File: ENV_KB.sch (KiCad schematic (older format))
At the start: 224 parts, among them J1 TYPE-C-31-M-12, J2 Conn_01x03, U1 MCP23017_SP

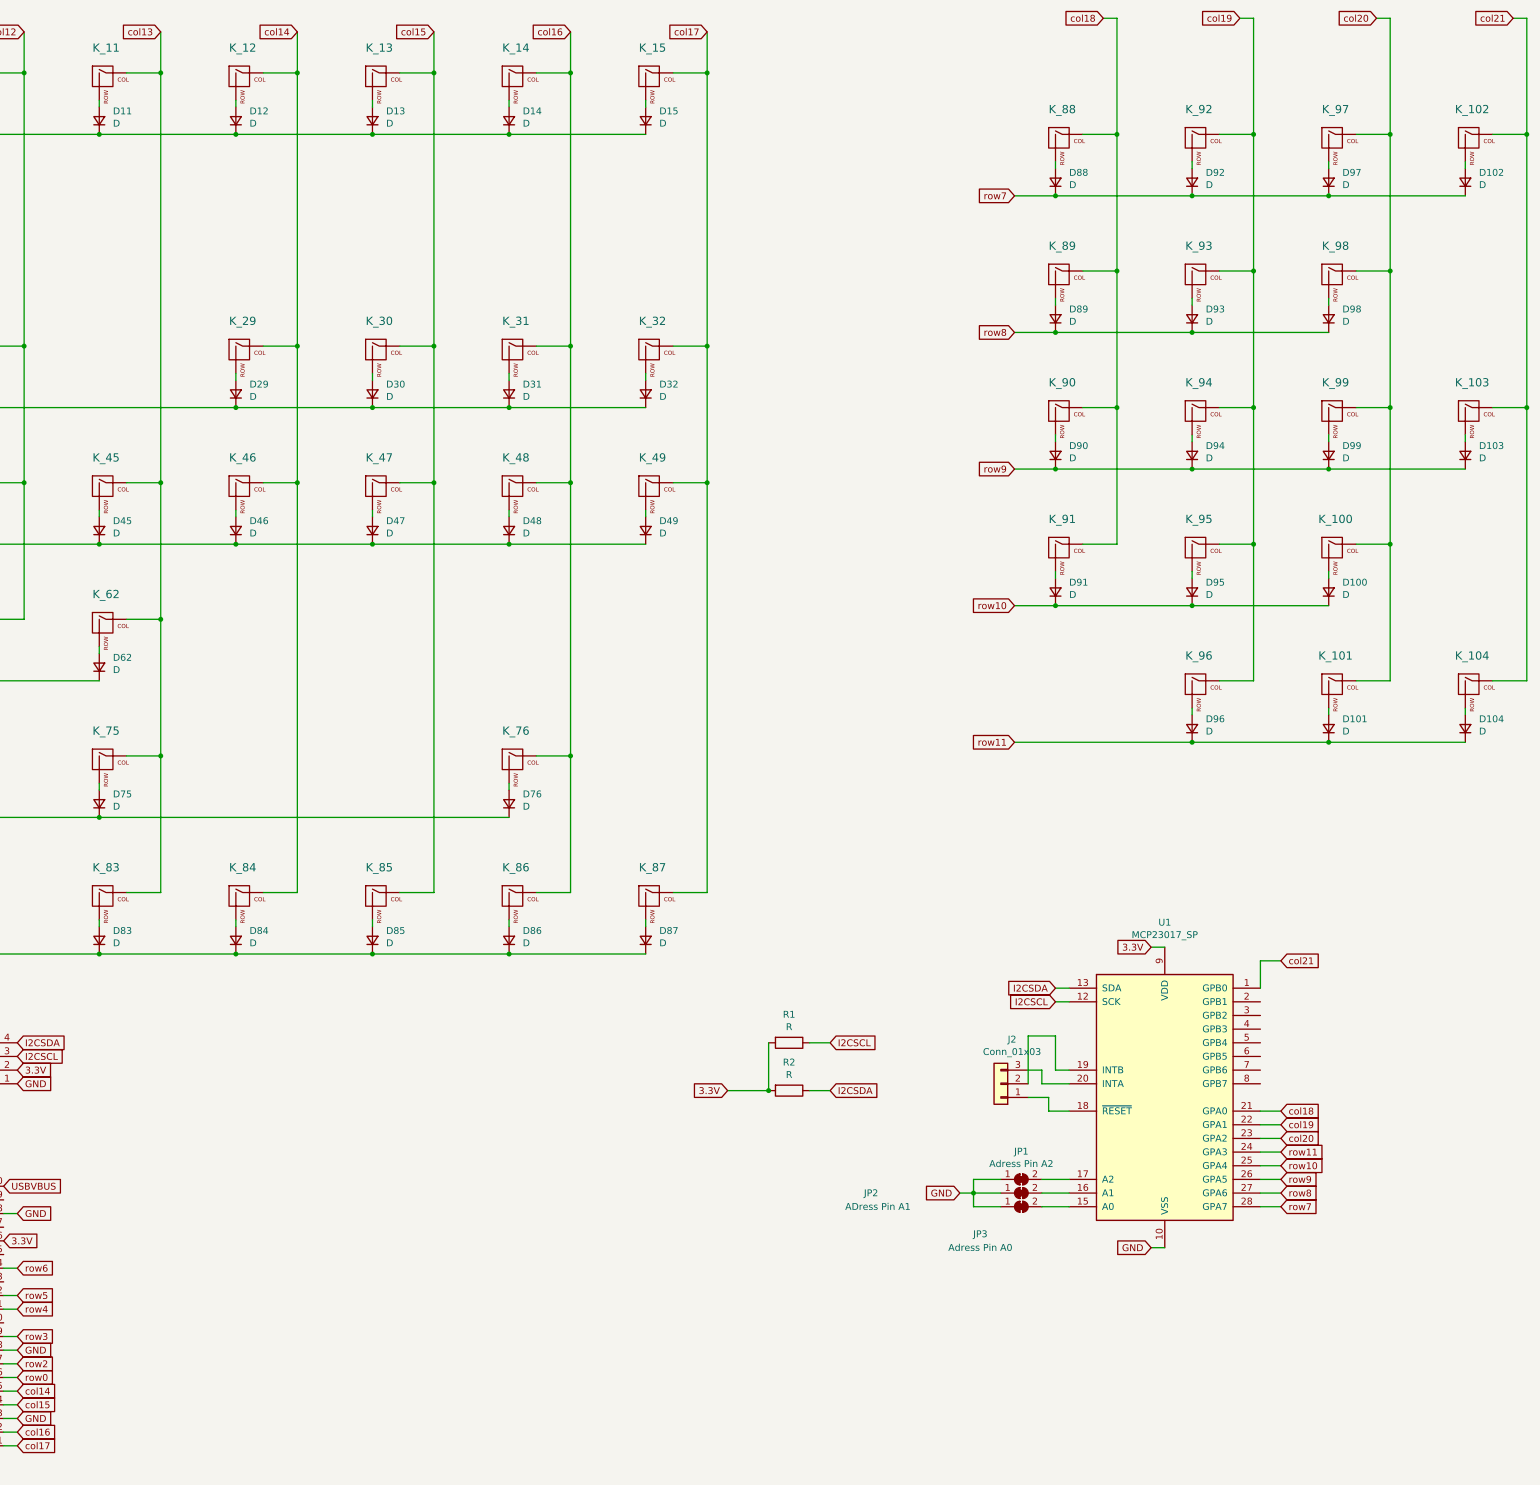
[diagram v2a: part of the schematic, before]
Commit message: Change: chaning schematic to use rows of main keyboard to save boot time TODO: Rerunning of the tracks to comply with schematic
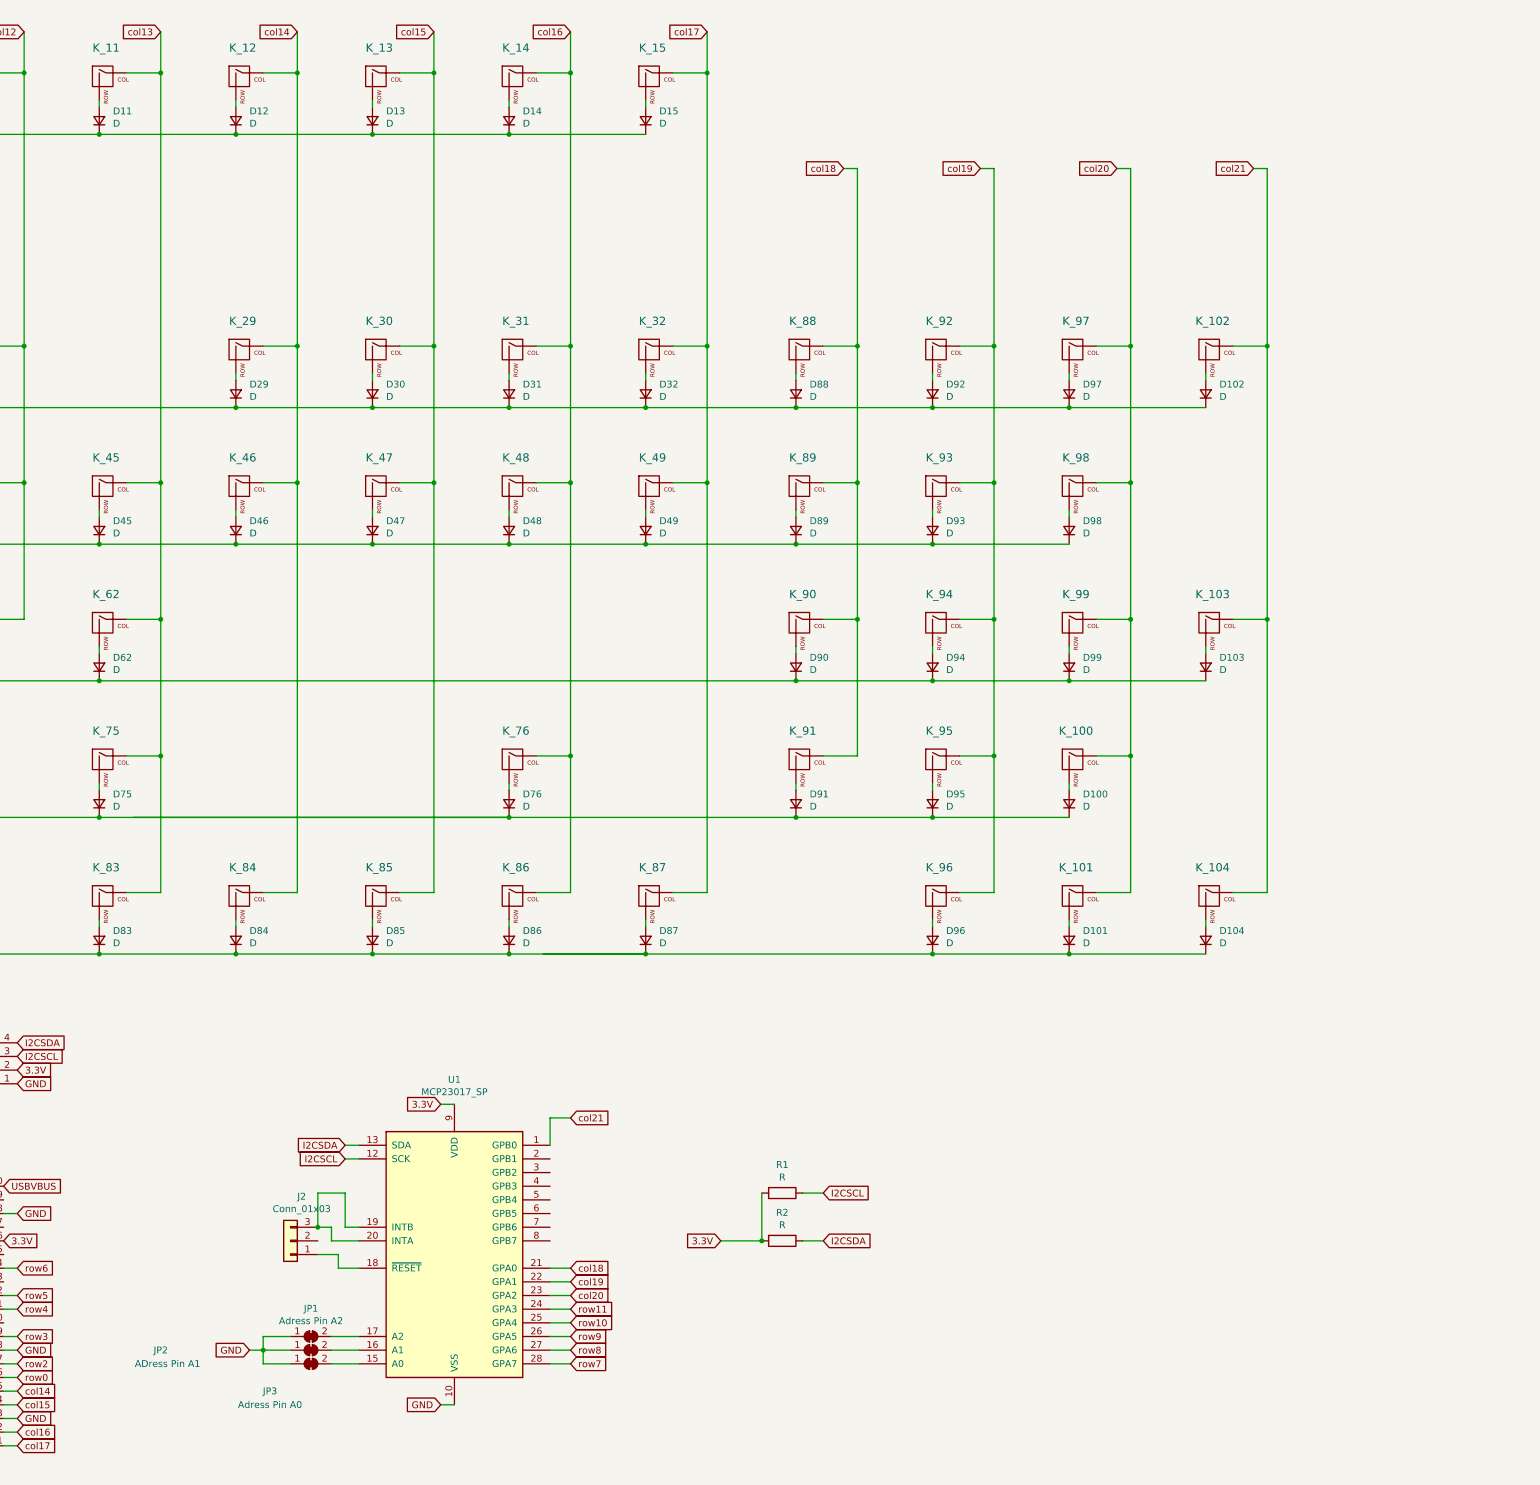
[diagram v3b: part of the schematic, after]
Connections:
- net row10: no longer D100.1 (K), D91.1 (K), D95.1 (K)
- net row11: no longer D101.1 (K), D104.1 (K), D96.1 (K)
- net row2: now also D102.1 (K), D88.1 (K), D92.1 (K), D97.1 (K)
- net row3: now also D89.1 (K), D93.1 (K), D98.1 (K)
- net row4: now also D103.1 (K), D90.1 (K), D94.1 (K), D99.1 (K)
- net row5: now also D100.1 (K), D91.1 (K), D95.1 (K)
- net row6: now also D101.1 (K), D104.1 (K), D96.1 (K)
- net row7: no longer D102.1 (K), D88.1 (K), D92.1 (K), D97.1 (K)
- net row8: no longer D89.1 (K), D93.1 (K), D98.1 (K)
- net row9: no longer D103.1 (K), D90.1 (K), D94.1 (K), D99.1 (K)
- net at U1.19 (INTB): now also J2.3 (Pin_3), U1.20 (INTA); no longer J2.2 (Pin_2)
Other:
- moved on the sheet: D100, D101, D102, D103, D104, D88, D89, D90, D91, D92, D93, D94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

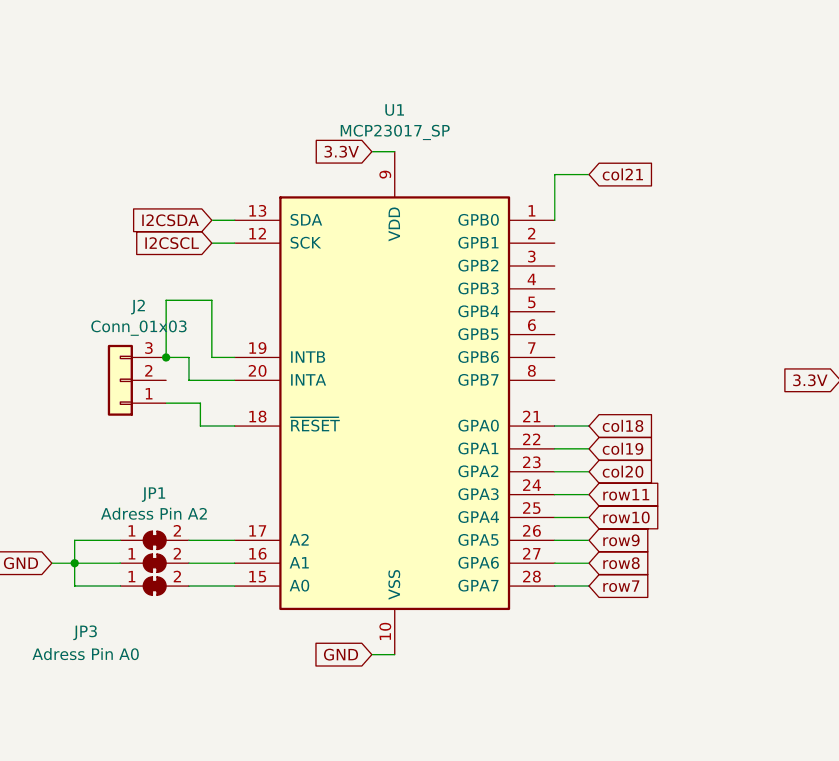
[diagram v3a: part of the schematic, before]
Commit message: Reouting Tracks Rerunning tacks to use Rows of main keyboard Update TO DO
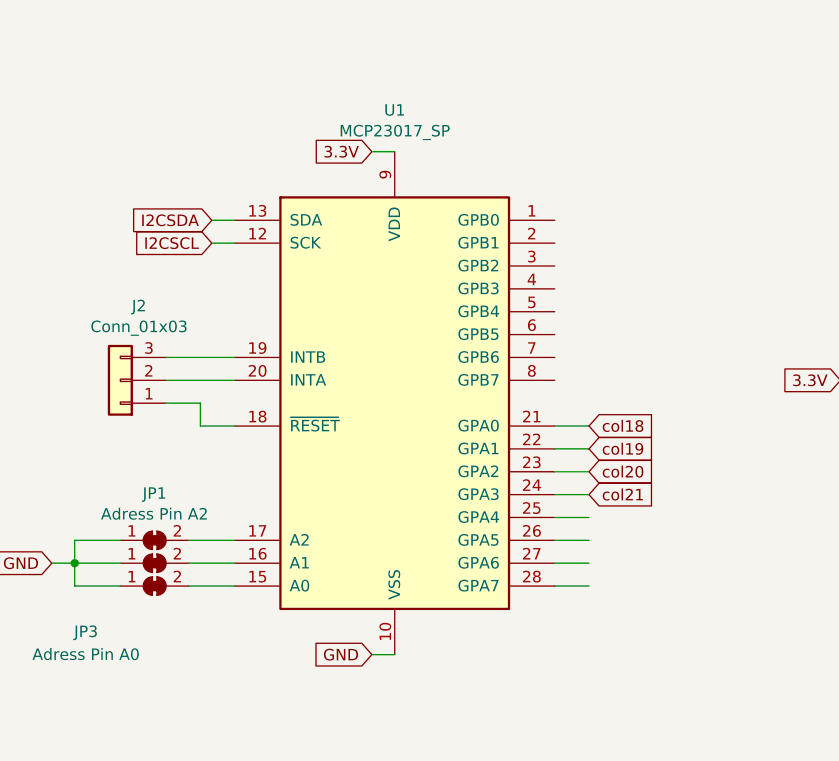
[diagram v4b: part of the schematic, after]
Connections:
- net row11 is gone; now on net col21: U1.24 (GPA3)
- net col21: no longer U1.1 (GPB0)
- net at J2.3 (Pin_3), U1.19 (INTB): no longer U1.20 (INTA)
- net at J2.2 (Pin_2): now also U1.20 (INTA)
- net row10: no longer names the net of U1.25 (GPA4)
- net row7: no longer names the net of U1.28 (GPA7)
- net row8: no longer names the net of U1.27 (GPA6)
- net row9: no longer names the net of U1.26 (GPA5)
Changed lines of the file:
@@
 Wire Wire Line
 	19450 4150 19450 4200
-Text GLabel 17800 10100 2    50   Input ~ 0
-row10
-Text GLabel 17800 10200 2    50   Input ~ 0
-row9
-Text GLabel 17800 10400 2    50   Input ~ 0
-row7
-Text GLabel 17800 10300 2    50   Input ~ 0
-row8
 Wire Wire Line
 	17800 10200 17650 10200
@@
 Wire Wire Line
 	17650 10000 17800 10000
-Text GLabel 17800 10000 2    50   Input ~ 0
-row11
 $Comp
 L Interface_Expansion:MCP23017_SP U?
@@
 Wire Wire Line
 	16100 9600 15950 9600
-Wire Wire Line
-	16050 9500 16050 9400
-Wire Wire Line
-	16050 9400 15950 9400
-Wire Wire Line
-	16250 9500 16050 9500
-Wire Wire Line
-	16250 9400 16150 9400
-Wire Wire Line
-	16150 9400 16150 9150
-Wire Wire Line
-	16150 9150 15950 9150
-Wire Wire Line
-	15950 9150 15950 9400
 $Comp
 L Jumper:SolderJumper_2_Bridged JP1
@@
 Text GLabel 18900 9500 0    50   Input ~ 0
 3.3V
-Text GLabel 17800 8600 2    50   Input ~ 0
+Text GLabel 17800 10000 2    50   Input ~ 0
 col21
-Wire Wire Line
-	17800 8600 17650 8600
-Wire Wire Line
-	17650 8600 17650 8800
 Connection ~ 19450 3400
 Wire Wire Line
@@
 	19900 1650 19900 2950
 Connection ~ 19900 2950
-Connection ~ 15950 9400
 Connection ~ 17350 6400
 Wire Wire Line
@@
 	18350 3400 19450 3400
 Connection ~ 18350 3400
+Wire Wire Line
+	15950 9400 16250 9400
+Wire Wire Line
+	15950 9500 16250 9500
 $EndSCHEMATC
